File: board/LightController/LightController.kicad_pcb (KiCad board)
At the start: 2 copper layers, 82.8 x 66 mm, 16 parts, among them J1 Jack-DC, J2 Light bank 1, J3 Light Bank 2, J4 Light Bank 3, U1 CPC1002N, U2 AP63205WU, U3 FeatherS2

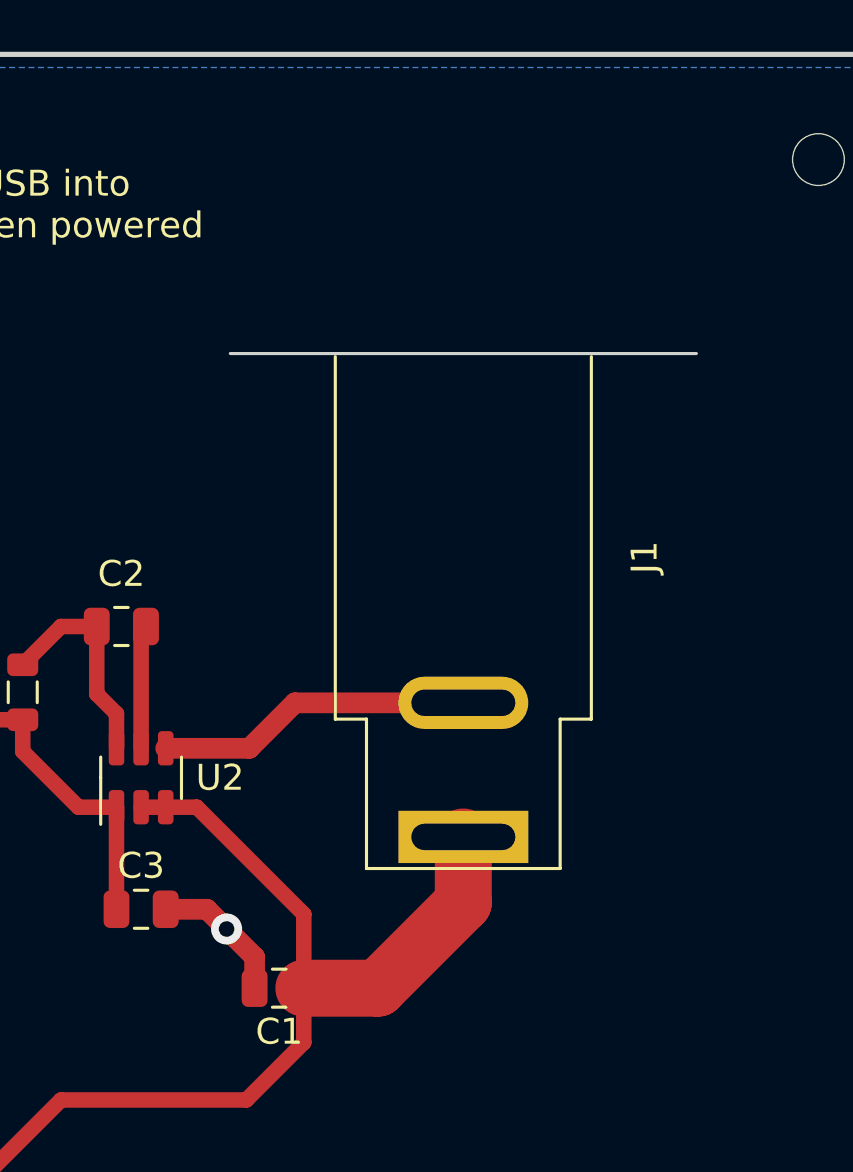
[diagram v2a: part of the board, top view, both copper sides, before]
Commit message: Using PJ-051AH barrel DC power jack.
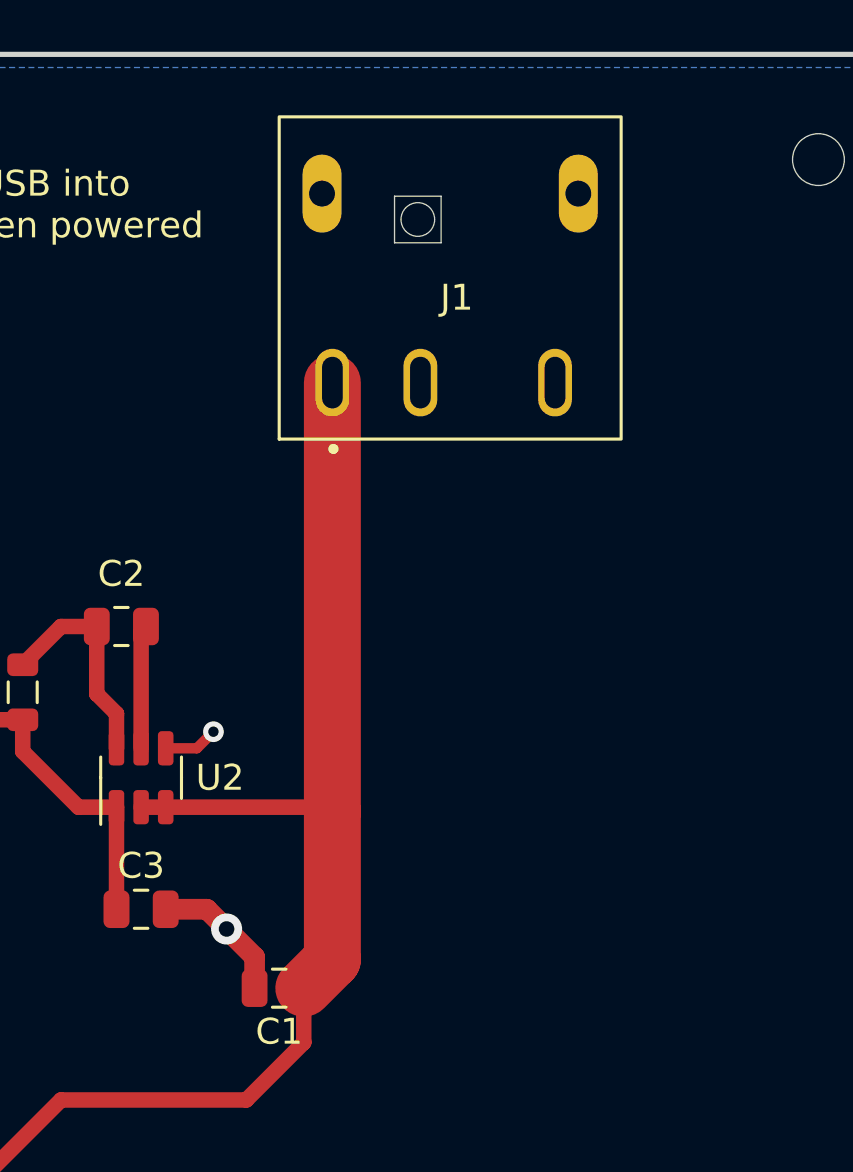
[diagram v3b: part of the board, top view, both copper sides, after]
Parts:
- J1: value Jack-DC -> PJ-051AH; footprint Connector_BarrelJack:BarrelJack_SwitchcraftConxall_RAPC10U_Horizontal -> cmumford:PJ-051AH
- moved J1 22.1 mm to (157.5, 56.6), turned to 90 degrees
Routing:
- net +24V: track 39.1 -> 49.4 mm
- net GND: track 29.3 -> 19.2 mm, vias 1 -> 2
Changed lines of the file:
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@@
   (net 41 "unconnected-(U3-Pad28)")
   (net 42 "Net-(R1-Pad1)")
+  (net 43 "unconnected-(J1-Pad3)")
+  (net 44 "unconnected-(J1-PadS1)")
+  (net 45 "unconnected-(J1-PadS2)")
   (footprint "Resistor_SMD:R_0805_2012Metric" (layer "F.Cu")
     (at 133.858 100.33)
@@
     (pad "" np_thru_hole circle (at 0 0) (size 2 2) (drill 2) (layers *.Cu *.Mask))
   )
-  (footprint "Connector_BarrelJack:BarrelJack_SwitchcraftConxall_RAPC10U_Horizontal" (layer "F.Cu")
-    (at 157.988 78.74 -90)
-    (descr "DC Power Jack, 13A, 24V, Panel Mount,Through-hole, https://www.switchcraft.com/Drawings/RAPC10U_CD.pdf")
-    (tags "barreljack switchcraftconxall dc power")
-    (property "Sheetfile" "LightController.kicad_sch")
-    (property "Sheetname" "")
-    (attr through_hole)
-    (fp_text reference "J1" (at -10.8 -7 90) (layer "F.SilkS")
-      (effects (font (size 1 1) (thickness 0.15)))
-    )
-    (fp_text value "Jack-DC" (at -11 9.9 90) (layer "F.Fab")
-      (effects (font (size 1 1) (thickness 0.15)))
-    )
-    (fp_text user "${REFERENCE}" (at -10.4 0 90) (layer "F.Fab")
-      (effects (font (size 1 1) (thickness 0.15)))
-    )
-    (fp_line (start -18.55 4.945) (end -4.55 4.945) (layer "F.SilkS") (width 0.12))
-    (fp_line (start -4.55 4.945) (end -4.55 3.74) (layer "F.SilkS") (width 0.12))
-    (fp_line (start -4.55 -4.945) (end -18.55 -4.945) (layer "F.SilkS") (width 0.12))
-    (fp_line (start -4.55 3.74) (end 1.22 3.74) (layer "F.SilkS") (width 0.12))
-    (fp_line (start 1.22 -3.74) (end -4.55 -3.74) (layer "F.SilkS") (width 0.12))
-    (fp_line (start 1.22 3.74) (end 1.22 -3.74) (layer "F.SilkS") (width 0.12))
-    (fp_line (start -4.55 -3.74) (end -4.55 -4.945) (layer "F.SilkS") (width 0.12))
-    (fp_line (start -18.67 -9) (end -18.67 9) (layer "Edge.Cuts") (width 0.12))
-    (fp_line (start -28.93 -6.47) (end 1.51 -6.47) (layer "F.CrtYd") (width 0.05))
-    (fp_line (start 1.51 6.47) (end -28.93 6.47) (layer "F.CrtYd") (width 0.05))
-    (fp_line (start 1.51 -6.47) (end 1.51 6.47) (layer "F.CrtYd") (width 0.05))
-    (fp_line (start -28.93 6.47) (end -28.93 -6.47) (layer "F.CrtYd") (width 0.05))
-    (fp_line (start -4.67 4.8) (end -4.67 3.62) (layer "F.Fab") (width 0.1))
-    (fp_line (start -20.17 -5.97) (end -18.77 -5.97) (layer "F.Fab") (width 0.1))
-    (fp_line (start -28.43 -4.065) (end -28.43 3.175) (layer "F.Fab") (width 0.1))
-    (fp_line (start -18.77 4.825) (end -4.67 4.825) (layer "F.Fab") (width 0.1))
-    (fp_line (start 0 3.62) (end 0 -3.62) (layer "F.Fab") (width 0.1))
-    (fp_line (start -20.17 -5.97) (end -20.17 5.97) (layer "F.Fab") (width 0.1))
-    (fp_line (start -18.77 -5.97) (end -18.77 5.97) (layer "F.Fab") (width 0.1))
-    (fp_line (start -4.67 -3.62) (end -4.67 -4.8) (layer "F.Fab") (width 0.1))
-    (fp_line (start -20.17 -4.065) (end -28.43 -4.065) (layer "F.Fab") (width 0.1))
-    (fp_line (start -18.77 -4.825) (end -4.67 -4.825) (layer "F.Fab") (width 0.1))
-    (fp_line (start -20.17 5.97) (end -18.77 5.97) (layer "F.Fab") (width 0.1))
-    (fp_line (start -28.43 3.175) (end -20.17 3.175) (layer "F.Fab") (width 0.1))
-    (fp_line (start 0 -3.62) (end -4.67 -3.62) (layer "F.Fab") (width 0.1))
-    (fp_line (start -4.67 3.62) (end 0 3.62) (layer "F.Fab") (width 0.1))
-    (pad "1" thru_hole rect (at 0 0 270) (size 2.02 5.02) (drill oval 1.02 4.02) (layers *.Cu *.Mask)
-      (net 1 "+24V") (pintype "passive"))
-    (pad "2" thru_hole oval (at -5.18 0 270) (size 2.02 5.02) (drill oval 1.02 4.02) (layers *.Cu *.Mask)
-      (net 2 "GND") (pintype "passive"))
-    (model "${KICAD6_3DMODEL_DIR}/Connector_BarrelJack.3dshapes/BarrelJack_SwitchcraftConxall_RAPC10U_Horizontal.wrl"
-      (offset (xyz 0 0 0))
-      (scale (xyz 1 1 1))
-      (rotate (xyz 0 0 0))
-    )
-  )
   (footprint "MountingHole:MountingHole_2mm" (layer "F.Cu")
     (at 171.704 110.49)
@@
     (pad "" np_thru_hole circle (at 0 0) (size 2 2) (drill 2) (layers *.Cu *.Mask))
   )
+  (footprint "cmumford:PJ-051AH" (layer "F.Cu")
+    (at 157.48 56.642 90)
+    (property "MANUFACTURER" "CUI Inc.")
+    (property "PARTREV" "1.03")
+    (property "STANDARD" "Manufacturer Recommendations")
+    (property "Sheetfile" "LightController.kicad_sch")
+    (property "Sheetname" "")
+    (attr through_hole)
+    (fp_text reference "J1" (at -1.27 0.254 180) (layer "F.SilkS")
+      (effects (font (size 1.000488 1.000488) (thickness 0.15)))
+    )
+    (fp_text value "PJ-051AH" (at -7.62 1.27 180) (layer "F.Fab")
+      (effects (font (size 1.001937 1.001937) (thickness 0.15)))
+    )
+    (fp_rect (start -6.731 -6.604) (end 5.715 6.604) (layer "F.SilkS") (width 0.12) (fill none))
+    (fp_circle (center -7.112 -4.51) (end -7.012 -4.51) (layer "F.SilkS") (width 0.2) (fill none))
+    (fp_line (start 2.65 -0.35) (end 0.85 -0.35) (layer "Edge.Cuts") (width 0.01))
+    (fp_line (start 0.85 -2.15) (end 2.65 -2.15) (layer "Edge.Cuts") (width 0.01))
+    (fp_line (start 0.85 -0.35) (end 0.85 -2.15) (layer "Edge.Cuts") (width 0.01))
+    (fp_line (start 2.65 -2.15) (end 2.65 -0.35) (layer "Edge.Cuts") (width 0.01))
+    (fp_line (start 1.2 5.45) (end 1.2 6.15) (layer "F.CrtYd") (width 0.05))
+    (fp_line (start 5.95 5.45) (end 5.95 -6) (layer "F.CrtYd") (width 0.05))
+    (fp_line (start 1.2 5.45) (end -6.223 5.45) (layer "F.CrtYd") (width 0.05))
+    (fp_line (start 5.95 -6) (end -6.223 -6) (layer "F.CrtYd") (width 0.05))
+    (fp_line (start -6.223 -6) (end -6.223 5.45) (layer "F.CrtYd") (width 0.05))
+    (fp_line (start 5.95 5.45) (end 4.45 5.45) (layer "F.CrtYd") (width 0.05))
+    (fp_line (start 4.45 6.15) (end 1.2 6.15) (layer "F.CrtYd") (width 0.05))
+    (fp_line (start 4.45 6.15) (end 4.45 5.45) (layer "F.CrtYd") (width 0.05))
+    (pad "" np_thru_hole circle (at 1.75 -1.25 90) (size 1.3 1.3) (drill 1.3) (layers *.Cu *.Mask))
+    (pad "1" thru_hole oval (at -4.55 -4.55 90) (size 2.616 1.308) (drill oval 2 0.8) (layers *.Cu *.Mask)
+      (net 1 "+24V") (pintype "passive"))
+    (pad "2" thru_hole oval (at -4.55 4.05 90) (size 2.616 1.308) (drill oval 2 0.8) (layers *.Cu *.Mask)
+      (net 2 "GND") (pintype "passive"))
+    (pad "3" thru_hole oval (at -4.55 -1.15 90) (size 2.616 1.308) (drill oval 2 0.8) (layers *.Cu *.Mask)
+      (net 43 "unconnected-(J1-Pad3)") (pintype "passive+no_connect"))
+    (pad "S1" thru_hole oval (at 2.75 -4.95 90) (size 3.016 1.508) (drill 1) (layers *.Cu *.Mask)
+      (net 44 "unconnected-(J1-PadS1)") (pinfunction "SHIELD") (pintype "passive+no_connect"))
+    (pad "S2" thru_hole oval (at 2.75 4.95 90) (size 3.016 1.508) (drill 1) (layers *.Cu *.Mask)
+      (net 45 "unconnected-(J1-PadS2)") (pinfunction "SHIELD") (pintype "passive+no_connect"))
+    (model "${CMUMFORD_COMPONENTS}/3dshapes/PJ-051AH.step"
+      (offset (xyz 6 0 0))
+      (scale (xyz 1 1 1))
+      (rotate (xyz 90 -180 90))
+    )
+  )
   (gr_rect (start 92.964 48.514) (end 175.768 114.554) (layer "Edge.Cuts") (width 0.2) (fill none))
   (gr_text "Bank 1" (at 144.272 109.474) (layer "F.SilkS")
@@
     (effects (font (size 1 1) (thickness 0.15)) (justify left))
   )
-  (segment (start 154.686 84.582) (end 157.988 81.28) (width 2.2) (layer "F.Cu") (net 1))
-  (segment (start 157.988 81.28) (end 157.988 78.74) (width 2.2) (layer "F.Cu") (net 1))
+  (segment (start 152.93 77.746) (end 152.93 83.478) (width 2.2) (layer "F.Cu") (net 1))
+  (segment (start 152.93 61.192) (end 152.93 77.746) (width 2.2) (layer "F.Cu") (net 1))
   (segment (start 149.606 88.9) (end 151.826 86.68) (width 0.6) (layer "F.Cu") (net 1))
   (segment (start 145.542 77.5915) (end 146.492 77.5915) (width 0.6) (layer "F.Cu") (net 1))
-  (segment (start 147.6955 77.5915) (end 151.826 81.722) (width 0.6) (layer "F.Cu") (net 1))
-  (segment (start 151.826 84.582) (end 154.686 84.582) (width 2.2) (layer "F.Cu") (net 1))
-  (segment (start 151.826 81.722) (end 151.826 84.582) (width 0.6) (layer "F.Cu") (net 1))
+  (segment (start 152.7755 77.5915) (end 152.93 77.746) (width 0.6) (layer "F.Cu") (net 1))
+  (segment (start 146.492 77.5915) (end 152.7755 77.5915) (width 0.6) (layer "F.Cu") (net 1))
   (segment (start 151.826 86.68) (end 151.826 84.582) (width 0.6) (layer "F.Cu") (net 1))
   (segment (start 138.386 92.964) (end 142.45 88.9) (width 0.6) (layer "F.Cu") (net 1))
-  (segment (start 146.492 77.5915) (end 147.6955 77.5915) (width 0.6) (layer "F.Cu") (net 1))
+  (segment (start 152.93 83.478) (end 151.826 84.582) (width 2.2) (layer "F.Cu") (net 1))
   (segment (start 142.45 88.9) (end 149.606 88.9) (width 0.6) (layer "F.Cu") (net 1))
-  (segment (start 151.484 73.56) (end 149.7275 75.3165) (width 0.8) (layer "F.Cu") (net 2))
+  (segment (start 146.492 75.3165) (end 147.6955 75.3165) (width 0.4) (layer "F.Cu") (net 2))
   (segment (start 149.926 83.378) (end 148.844 82.296) (width 0.8) (layer "F.Cu") (net 2))
   (segment (start 134.7705 100.33) (end 135.89 100.33) (width 0.25) (layer "F.Cu") (net 2))
@@
   (segment (start 148.082 81.534) (end 148.844 82.296) (width 0.8) (layer "F.Cu") (net 2))
   (segment (start 146.492 81.534) (end 148.082 81.534) (width 0.8) (layer "F.Cu") (net 2))
+  (segment (start 147.6955 75.3165) (end 148.336 74.676) (width 0.4) (layer "F.Cu") (net 2))
   (segment (start 135.89 100.33) (end 141.229 105.669) (width 0.25) (layer "F.Cu") (net 2))
   (segment (start 141.229 105.669) (end 144.272 105.669) (width 0.25) (layer "F.Cu") (net 2))
-  (segment (start 157.988 73.56) (end 151.484 73.56) (width 0.8) (layer "F.Cu") (net 2))
-  (segment (start 149.7275 75.3165) (end 146.492 75.3165) (width 0.8) (layer "F.Cu") (net 2))
+  (via (at 148.336 74.676) (size 0.8) (drill 0.4) (layers "F.Cu" "B.Cu") (free) (net 2))
   (via (at 148.844 82.296) (size 1.2) (drill 0.6) (layers "F.Cu" "B.Cu") (net 2))
   (segment (start 145.542 75.3165) (end 145.542 70.8) (width 0.6) (layer "F.Cu") (net 3))

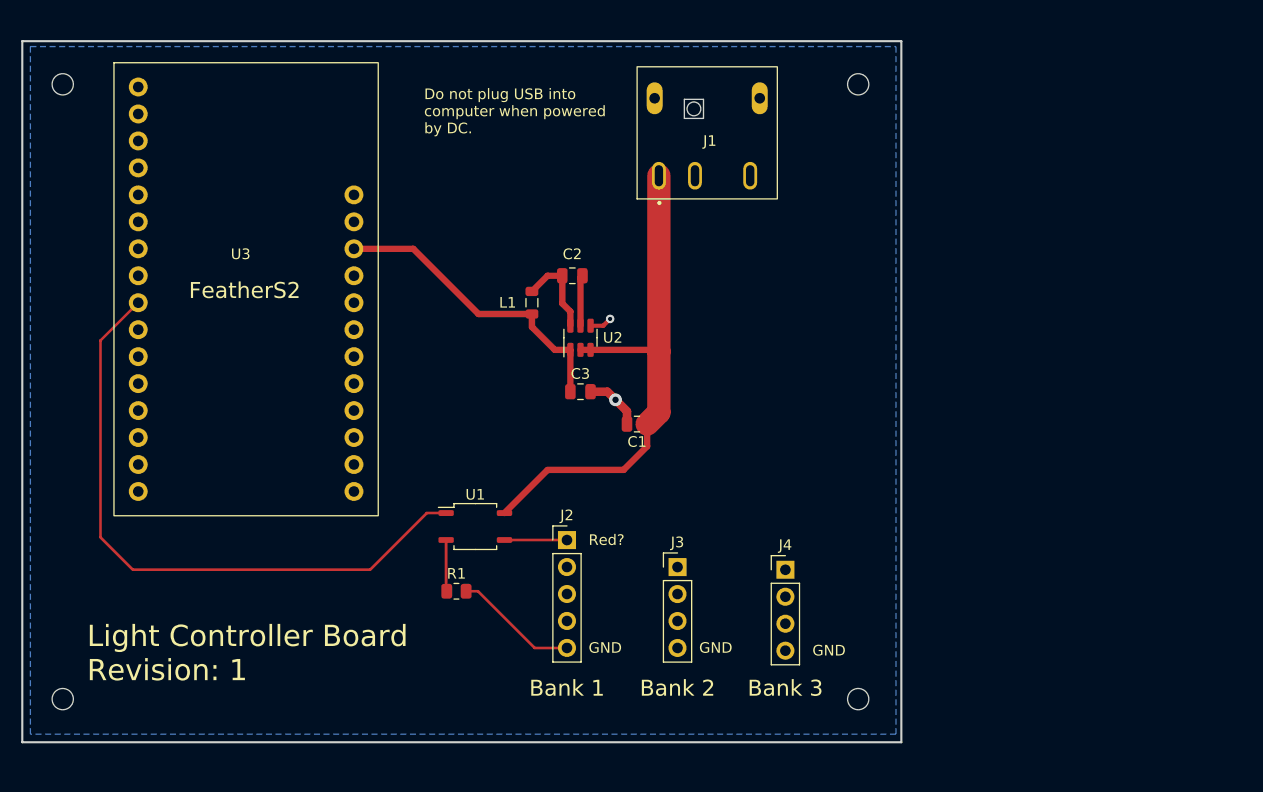
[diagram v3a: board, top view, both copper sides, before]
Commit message: All 10 relays.
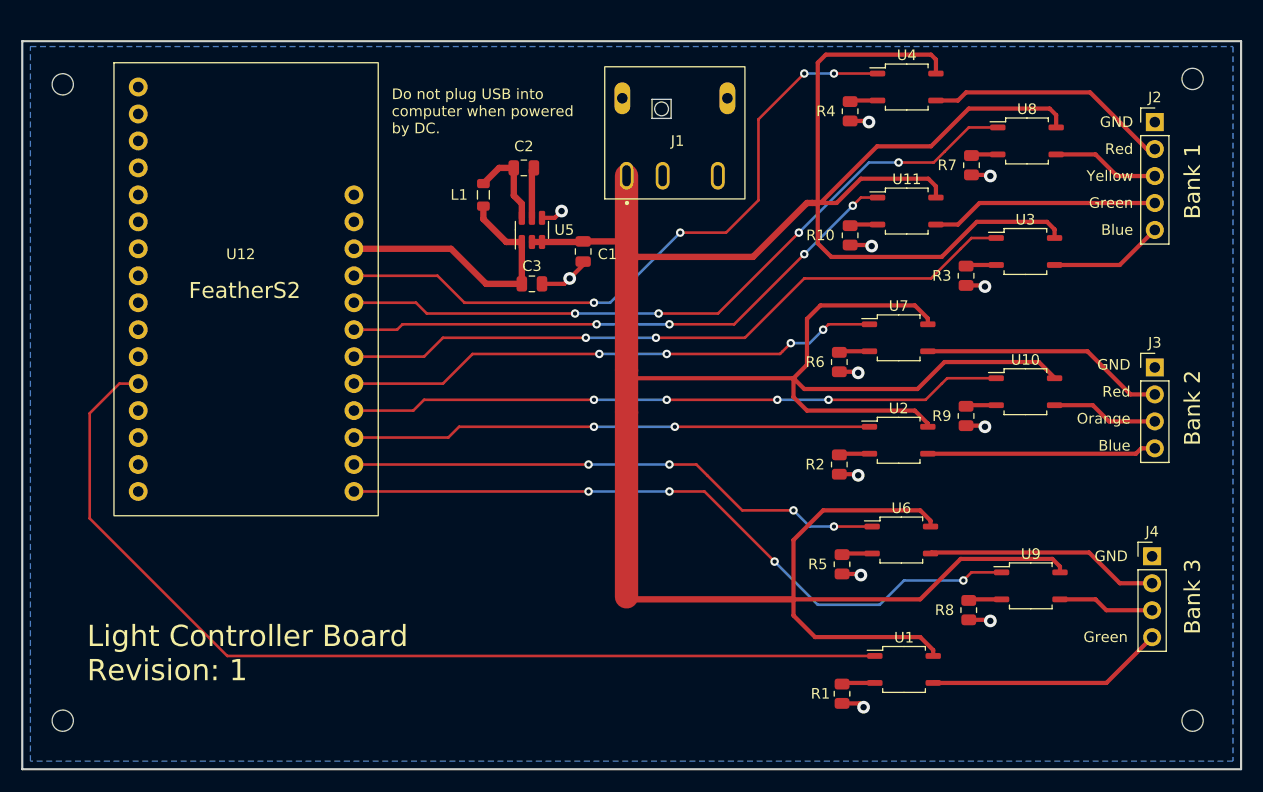
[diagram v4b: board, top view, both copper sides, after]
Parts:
- added R1: 3K3, Resistor_SMD:R_0805_2012Metric, F.Cu at (170.2, 110.0)
- added R10: 3K3, Resistor_SMD:R_0805_2012Metric, F.Cu at (170.9, 66.8)
- added R2: 3K3, Resistor_SMD:R_0805_2012Metric, F.Cu at (169.9, 88.4)
- added R3: 3K3, Resistor_SMD:R_0805_2012Metric, F.Cu at (181.9, 70.6)
- added R5: 3K3, Resistor_SMD:R_0805_2012Metric, F.Cu at (170.2, 97.8)
- added R6: 3K3, Resistor_SMD:R_0805_2012Metric, F.Cu at (169.9, 78.7)
- added R7: 3K3, Resistor_SMD:R_0805_2012Metric, F.Cu at (182.4, 60.2)
- added R8: 3K3, Resistor_SMD:R_0805_2012Metric, F.Cu at (182.1, 102.1)
- added R9: 3K3, Resistor_SMD:R_0805_2012Metric, F.Cu at (181.9, 83.8)
- added U1: CPC1002N, Package_SO:SOP-4_3.8x4.1mm_P2.54mm, F.Cu at (176.0, 107.7)
- added U10: CPC1002N, Package_SO:SOP-4_3.8x4.1mm_P2.54mm, F.Cu at (187.5, 81.5)
- added U11: CPC1002N, Package_SO:SOP-4_3.8x4.1mm_P2.54mm, F.Cu at (176.3, 64.5)
- added U2: CPC1002N, Package_SO:SOP-4_3.8x4.1mm_P2.54mm, F.Cu at (175.5, 86.1)
- added U3: CPC1002N, Package_SO:SOP-4_3.8x4.1mm_P2.54mm, F.Cu at (187.5, 68.3)
- added U6: CPC1002N, Package_SO:SOP-4_3.8x4.1mm_P2.54mm, F.Cu at (175.8, 95.5)
- added U7: CPC1002N, Package_SO:SOP-4_3.8x4.1mm_P2.54mm, F.Cu at (175.5, 76.5)
- added U8: CPC1002N, Package_SO:SOP-4_3.8x4.1mm_P2.54mm, F.Cu at (187.6, 57.9)
- added U9: CPC1002N, Package_SO:SOP-4_3.8x4.1mm_P2.54mm, F.Cu at (188.0, 99.8)
- moved J2 67.9 mm to (199.6, 56.1)
- moved R4 58.5 mm to (170.9, 55.1), turned to -90 degrees
- moved U4 58.0 mm to (176.3, 52.8)
- moved J3 48.7 mm to (199.6, 79.2)
- moved J4 34.6 mm to (199.4, 97.0)
- moved H2 31.6 mm to (203.2, 112.5)
- moved H1 31.5 mm to (203.2, 52.1)
- moved C1 17.0 mm to (145.8, 68.3), turned to -90 degrees
- moved C3 11.1 mm to (141.0, 71.4)
- moved L1 11.1 mm to (136.4, 63.0)
- moved C2 11.1 mm to (140.2, 60.5)
- moved U5 11.1 mm to (141.0, 66.3)
- moved J1 3.05 mm to (154.4, 56.6)
- moved H4 2.03 mm to (96.8, 112.5)
- renumbered R1 to R4, U3 to U12, U1 to U4, U2 to U5
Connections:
- J2 pad 1: LIGHT1_VIN -> GND
- J2 pad 2: unconnected-(J2-Pad2) -> LIGHT1_VIN
- J2 pad 3: unconnected-(J2-Pad3) -> LIGHT2_VIN
- J2 pad 4: unconnected-(J2-Pad4) -> LIGHT3_VIN
- J2 pad 5: GND -> LIGHT4_VIN
- J3 pad 1: unconnected-(J3-Pad1) -> GND
- J3 pad 2: unconnected-(J3-Pad2) -> LIGHT5_VIN
- J3 pad 3: unconnected-(J3-Pad3) -> LIGHT6_VIN
- J3 pad 4: GND -> LIGHT7_VIN
- J4 pad 1: unconnected-(J4-Pad1) -> GND
- J4 pad 2: unconnected-(J4-Pad2) -> LIGHT8_VIN
- J4 pad 3: unconnected-(J4-Pad3) -> LIGHT9_VIN
- J4 pad 4: GND -> LIGHT10_VIN
- U12 pad 12: unconnected-(U3-Pad12) -> LIGHT10_CTL
- U12 pad 17: unconnected-(U3-Pad17) -> LIGHT9_CTL
- U12 pad 18: unconnected-(U3-Pad18) -> LIGHT8_CTL
- U12 pad 19: unconnected-(U3-Pad19) -> LIGHT7_CTL
- U12 pad 20: unconnected-(U3-Pad20) -> LIGHT6_CTL
- U12 pad 21: unconnected-(U3-Pad21) -> LIGHT5_CTL
- U12 pad 22: unconnected-(U3-Pad22) -> LIGHT4_CTL
- U12 pad 23: unconnected-(U3-Pad23) -> LIGHT3_CTL
- U12 pad 24: unconnected-(U3-Pad24) -> LIGHT2_CTL
- U12 pad 25: unconnected-(U3-Pad25) -> LIGHT1_CTL
- U12 pad 9: LIGHT1_CTL -> unconnected-(U12-Pad9)
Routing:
- net +24V: track 49.4 -> 323.7 mm
- net LIGHT10_CTL: track 0.00 -> 95.0 mm
- net LIGHT2_CTL: track 0.00 -> 68.3 mm, vias 0 -> 4
- net LIGHT9_CTL: track 0.00 -> 66.7 mm, vias 0 -> 4
- net LIGHT4_CTL: track 0.00 -> 65.1 mm, vias 0 -> 2
- net LIGHT6_CTL: track 0.00 -> 61.8 mm, vias 0 -> 4
- net LIGHT3_CTL: track 0.00 -> 54.5 mm, vias 0 -> 4
- net LIGHT8_CTL: track 0.00 -> 51.2 mm, vias 0 -> 4
- net LIGHT5_CTL: track 0.00 -> 50.9 mm, vias 0 -> 4
- net LIGHT7_CTL: track 0.00 -> 49.0 mm, vias 0 -> 2
- net LIGHT5_VIN: track 0.00 -> 23.1 mm
- net LIGHT10_VIN: track 0.00 -> 22.4 mm
- net LIGHT8_VIN: track 0.00 -> 22.1 mm
- net LIGHT7_VIN: track 0.00 -> 21.6 mm
- net LIGHT3_VIN: track 0.00 -> 21.5 mm
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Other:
- board size 82.8 x 66 mm -> 114.8 x 68.6 mm
- board text added: "Blue"
- board text added: "Green"
- board text added: "Orange"
- board text added: "Red"
- board text added: "Yellow"
- board text removed: "Red?"
